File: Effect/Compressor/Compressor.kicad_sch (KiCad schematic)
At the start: 48 parts, among them J1 Conn_01x04_Pin, J2 Conn_01x04_Pin, Q1 MMBF5103, Q2 NMB2227A, Q3 MMBF5103, Q4 MMBF5103

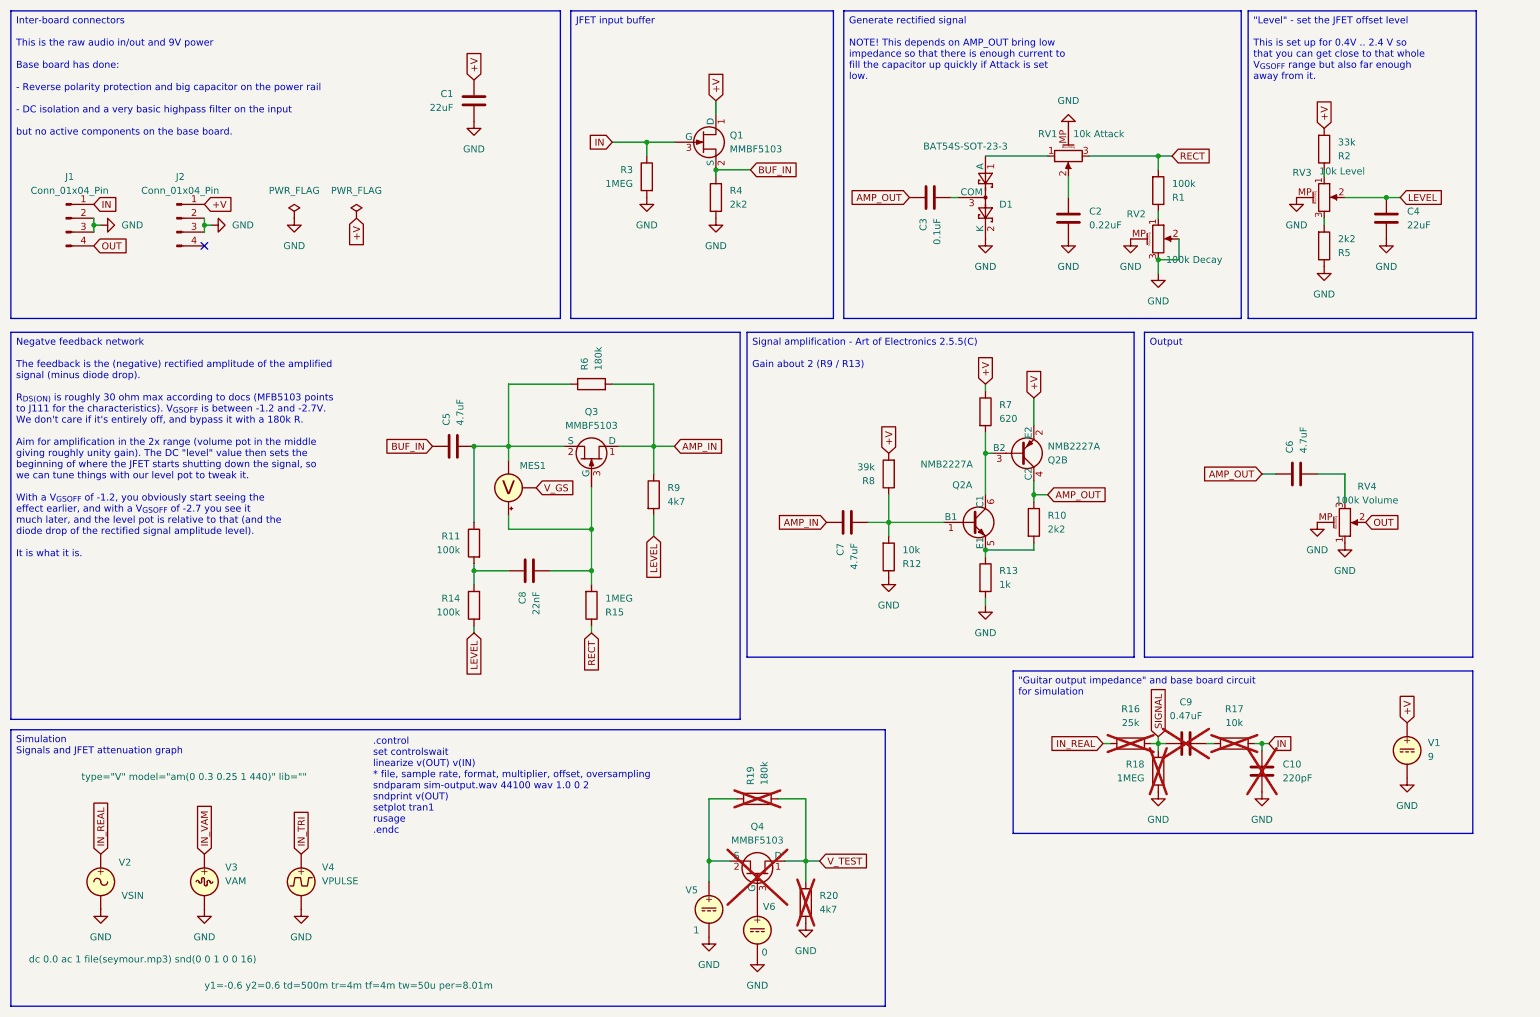
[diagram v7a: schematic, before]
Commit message: More compressor games
It turns ou tthat using the JFET to pass the signal (that I was so happy
about in commit c25f662: "Compressor: re-do with feedback loop and a
whole new approach") isn't so great after all.

In particular, it causes a kind of "zero-crossing distortion" where it
does compress the signal, but it does so by mainly compressing the
middle part, not the high ends.  Which looks all kinds of bad and
probably sounds worse.

I'm not 100% sure of the reason (I suspect there's some V_{DS} drop
effect), but clearly my clever trick was anything but.

Anyway, I do feel like I'm understanding how the JFET works much better
now, and I went back to the model with the JFET pulling the signal down,
and with my new-found understanding (famous last words) that looks a lot
better.

The whole "use a pot to set the voltage level" ended up making that
approach simpler too, because we don't now have to amplify the signal to
get that negative voltage with a diode/capacitor voltage inverter thing.
We can just adjust the level upwards to get a bigger V_{GS} drop..

This still does obviously amplify the signal, because we obviously don't
want to have a compressor that only makes the signal overall quieter.

I really would like to have a LED that shows when we start actually
compressing, but I'm still thinking about how to do that reasonably.

Signed-off-by: Linus Torvalds <torvalds@linux-foundation.org>
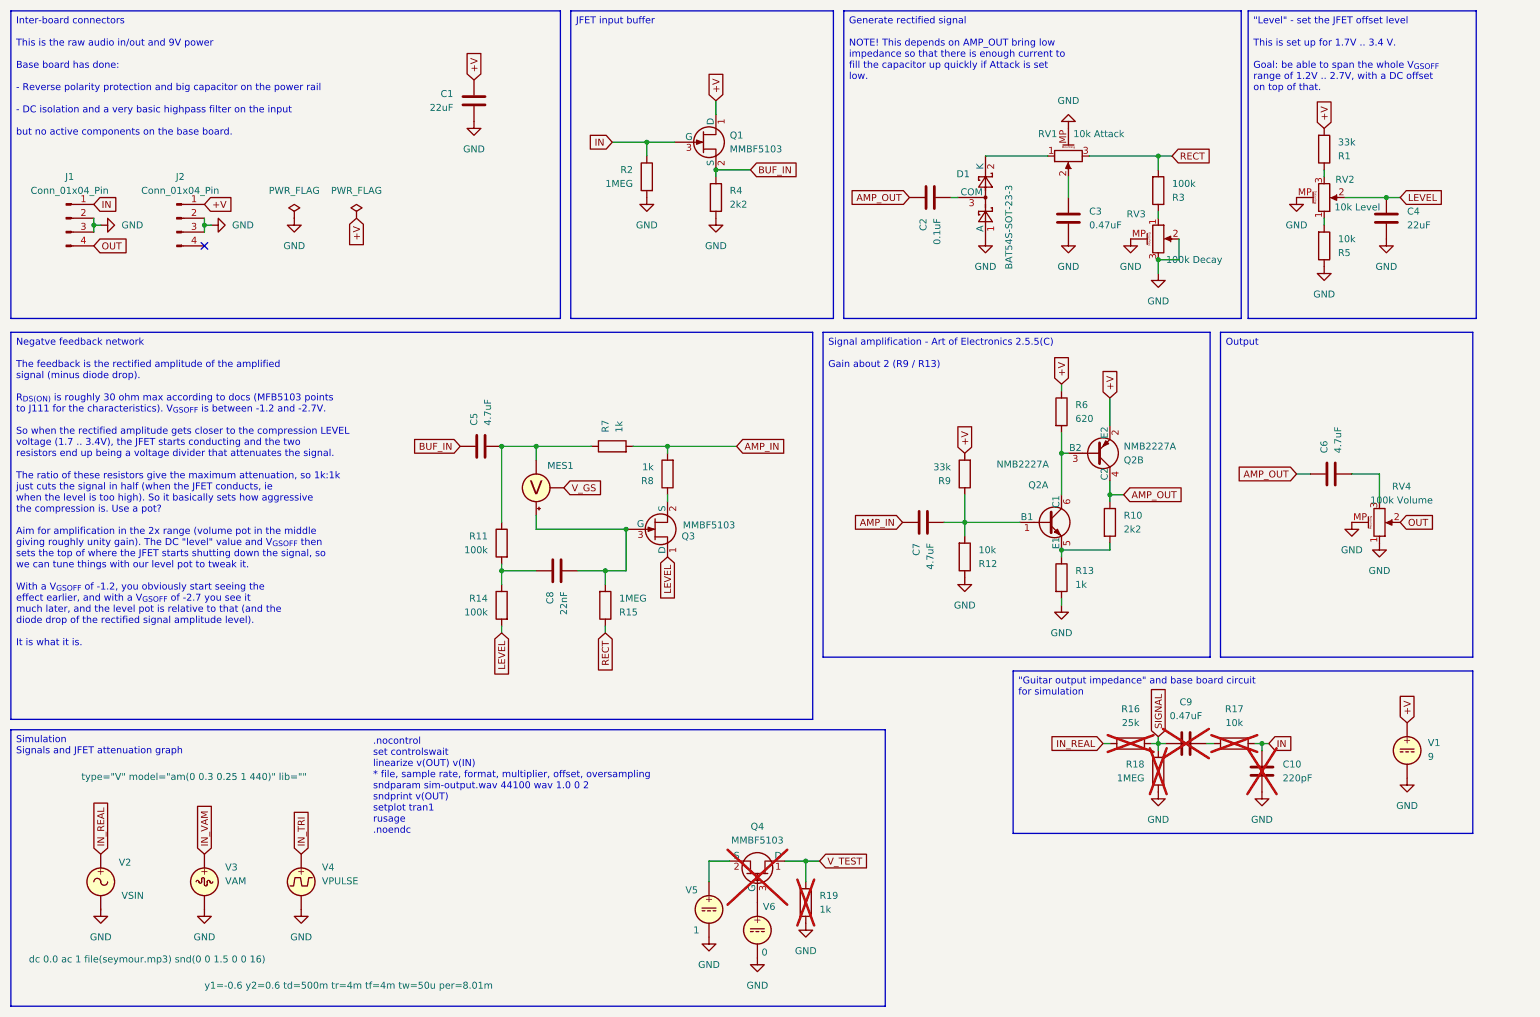
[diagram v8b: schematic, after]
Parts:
- removed R19, R6: 180k, Resistor_SMD:R_0805_2012Metric, symbol Device:R
- removed R9: 4k7, Resistor_SMD:R_0805_2012Metric, symbol Device:R
- added R7, R8: 1k, Resistor_SMD:R_0805_2012Metric, symbol Device:R
- C3: renamed from C2; value 0.22uF -> 0.47uF
- R19: renamed from R20; value 4k7 -> 1k
- R5: value 2k2 -> 10k
- R9: renamed from R8; value 39k -> 33k
- renumbered C3 to C2, R2 to R1, R3 to R2, R1 to R3, R7 to R6, RV3 to RV2, RV2 to RV3
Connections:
- net AMP_IN: now also R7.2, R8.2; no longer Q3.1 (D)
- net GND: now also D1.1 (A); no longer D1.2 (K)
- net LEVEL: now also Q3.1 (D)
- net at C5.2, MES1.2 (-), R11.1: now also R7.1; no longer Q3.2 (S)
- net at R5.2: now also RV2.1; no longer RV2.3
- net at RV1.1: now also D1.2 (K); no longer D1.1 (A)
- net at R1.1: now also RV2.3; no longer RV2.1
- new net: Q3.2 (S), R8.1
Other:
- note added: ".nocontrol set controlswait linearize v(OUT) v(IN) * file, sample rate, format, multiplier, offset, oversampling sndparam sim-output.wav 44100 wav 1.0 0 2 sndprint v(OUT) setplot tran1 rusage .noendc"
- note removed: ".control set controlswait linearize v(OUT) v(IN) * file, sample rate, format, multiplier, offset, oversampling sndparam sim-output.wav 44100 wav 1.0 0 2 sndprint v(OUT) setplot tran1 rusage .endc"
- moved on the sheet: C5, C6, C7, C8, MES1, Q2A, Q2B, Q3, R10, R11, R12, R13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
